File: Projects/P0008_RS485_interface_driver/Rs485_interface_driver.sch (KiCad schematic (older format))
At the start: 6 parts, among them J1 22-05-7045, J2 22-05-7045, U1 SN65176BDR, U2 78L05

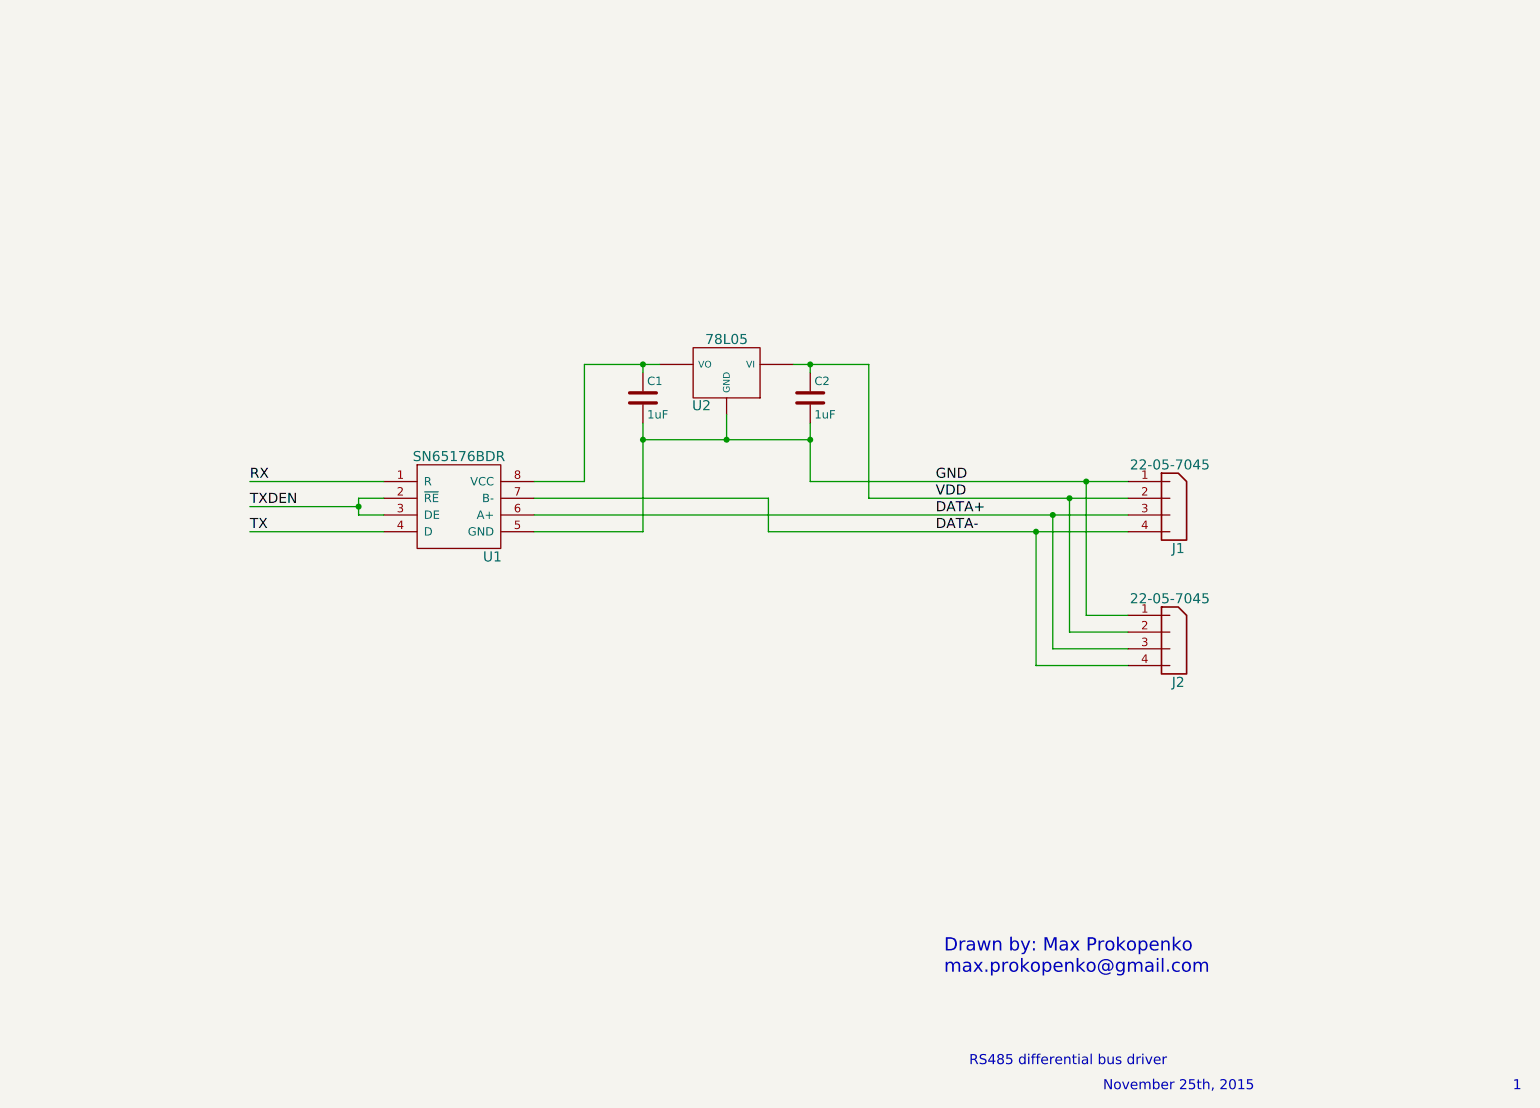
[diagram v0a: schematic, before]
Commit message: finishing routing on bus adapter
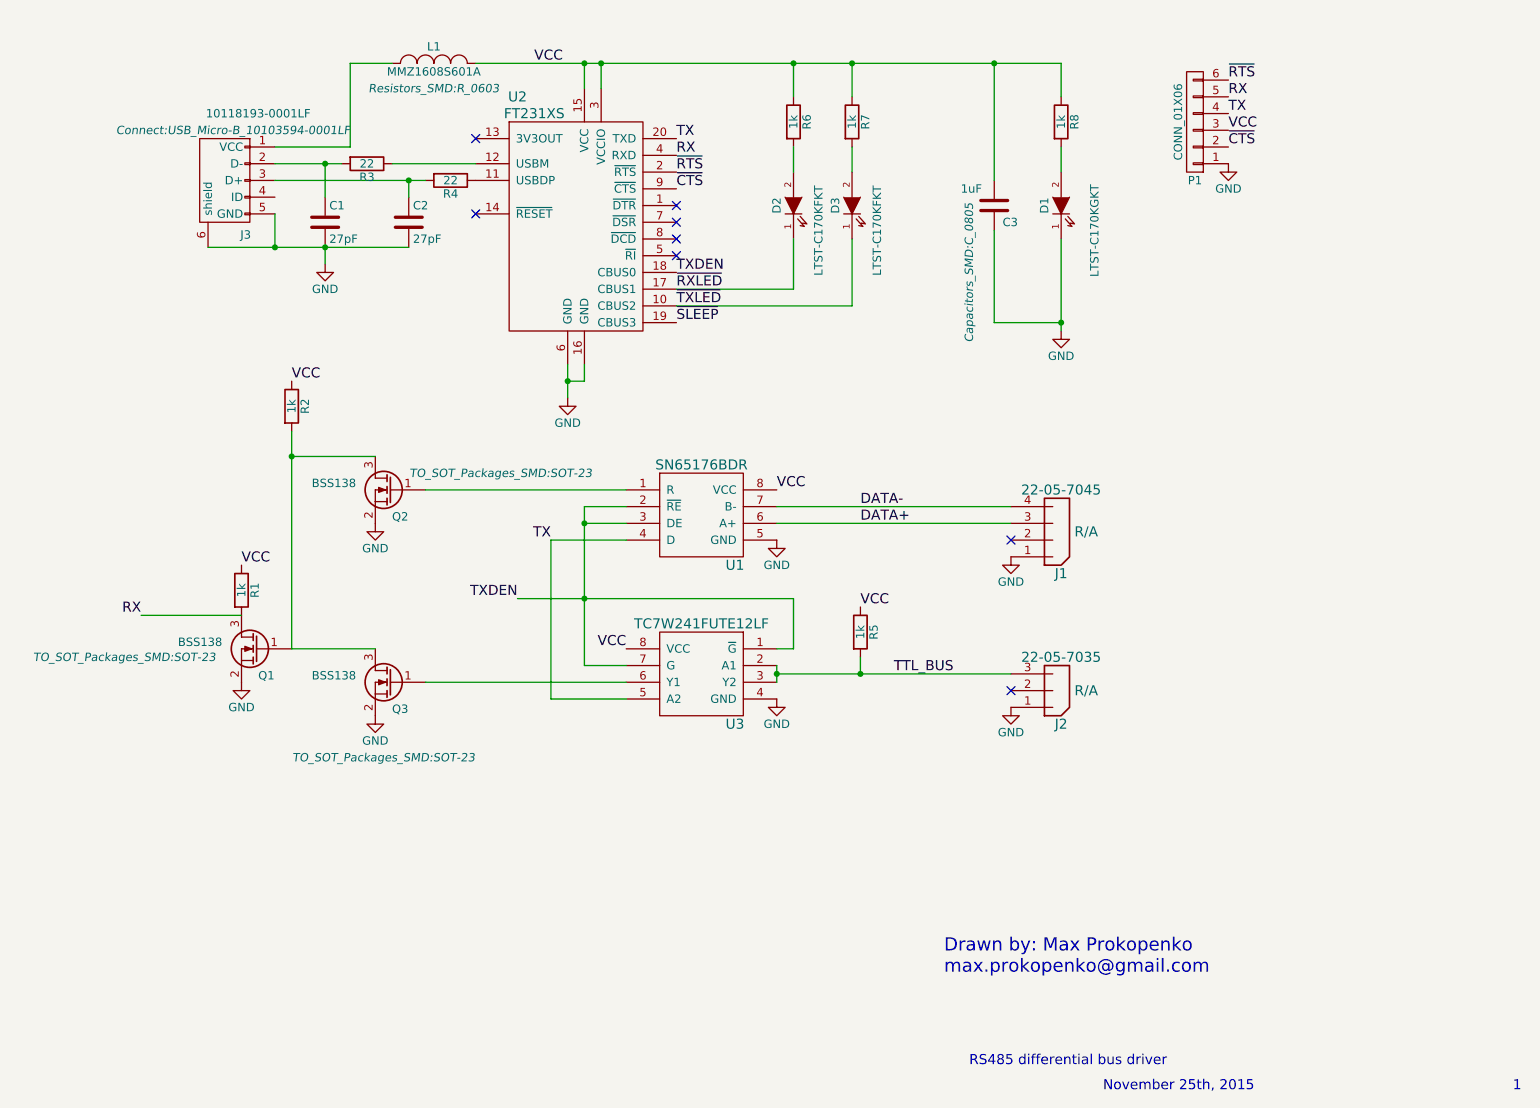
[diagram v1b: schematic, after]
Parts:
- removed J2: 22-05-7045, symbol 22-05-7045
- removed U2: 78L05, symbol 78L05
- added C3: 1uF, Capacitors_SMD:C_0805, symbol C
- added D1: LTST-C170KGKT, LEDs:LED_0805, symbol LTST-C170KGKT
- added D2, D3: LTST-C170KFKT, LEDs:LED_0805, symbol LTST-C170KFKT
- added J2: 22-05-7035, Pin_Headers:Pin_Header_Angled_1x03, symbol 22-05-7035
- added J3: 10118193-0001LF, Connect:USB_Micro-B_10103594-0001LF, symbol 10118193-0001LF
- added L1: MMZ1608S601A, Resistors_SMD:R_0603, symbol MMZ1608S601A
- added P1: CONN_01X06, Pin_Headers:Pin_Header_Straight_1x06, symbol CONN_01X06
- added Q1, Q2, Q3: BSS138, TO_SOT_Packages_SMD:SOT-23, symbol BSS138
- added R1, R2, R5, R6, R7, R8: 1k, Resistors_SMD:R_0805, symbol R
- added R3, R4: 22, Resistors_SMD:R_0805, symbol R
- added U2: FT231XS, SMD_Packages:SSOP-20, symbol FT231XS
- added U3: TC7W241FUTE12LF, Housings_SSOP:MSOP-8_3x3mm_Pitch0.65mm, symbol TC7W241FUTE12LF
- C1, C2: value 1uF -> 27pF; footprint (none) -> Capacitors_SMD:C_0402
- J1: footprint (none) -> Pin_Headers:Pin_Header_Angled_1x04; Orientation (none) -> R/A
- U1: footprint (none) -> Housings_SOIC:SOIC-8_3.9x4.9mm_Pitch1.27mm
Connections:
- net GND: now also C3.2, D1.1 (K), J2.1, J3.5 (GND), J3.6 (shield), P1.1 (P1), Q1.2 (S), Q2.2 (S), Q3.2 (S), U2.16 (GND), U2.6 (GND), U3.4 (GND)
- net RX: now also P1.5 (P5), Q1.3 (D), R1.2, U2.4 (RXD); no longer U1.1 (R)
- net TX: now also P1.4 (P4), U2.20 (TXD), U3.5 (A2)
- net TXDEN: now also U2.18 (CBUS0), U3.1 (~G), U3.7 (G)
- net at C1.1: now also J3.2 (D-), R3.2; no longer U1.8 (VCC)
- net VDD: no longer names the net of J1.2
- net VDD: no longer C2.1
- new net: Q2.1 (G), U1.1 (R)
- new net: Q3.1 (G), U3.6 (Y1)
- new net: Q1.1 (G), Q2.3 (D), Q3.3 (D), R2.2
- new net: J3.1 (VCC), L1.1
- new net: C2.1, J3.3 (D+), R4.2
- new net: R4.1, U2.11 (USBDP)
- new net: R3.1, U2.12 (USBM)
- new net: D2.2 (A), R6.2
- new net: D3.2 (A), R7.2
- new net: D1.2 (A), R8.2
- new net TTL_BUS: J2.3, R5.2, U3.2 (A1), U3.3 (Y2)
- new net VCC: C3.1, L1.2, P1.3 (P3), R1.1, R2.1, R5.1, R6.1, R7.1, R8.1, U1.8 (VCC), U2.15 (VCC), U2.3 (VCCIO), U3.8 (VCC)
- new net ~CTS: P1.2 (P2), U2.9 (~CTS)
- new net ~RTS: P1.6 (P6), U2.2 (~RTS)
- new net ~RXLED: D2.1 (K), U2.17 (CBUS1)
- new net ~SLEEP: U2.19 (CBUS3)
- new net ~TXLED: D3.1 (K), U2.10 (CBUS2)
- no-connect marks 0 -> 8
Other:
- moved on the sheet: U1

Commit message: revised P0008, added gerbers
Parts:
- removed Q2, Q3: BSS138, TO_SOT_Packages_SMD:SOT-23, symbol BSS138
- added Q2, Q3, Q4: BSS84, TO_SOT_Packages_SMD:SOT-23, symbol BSS84
- added R9: 1k, Resistors_SMD:R_0805, symbol R
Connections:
- net GND: now also R2.2
- net RX: no longer P1.5 (P5)
- net VCC: now also Q2.2 (S), Q3.2 (S), Q4.2 (S), R9.1; no longer R2.1
- net at U1.1 (R): now also Q3.1 (G)
- net at U3.6 (Y1): now also Q4.1 (G)
- net at Q1.1 (G): now also R2.1, Q2.3 (D), Q3.3 (D), Q4.3 (D); no longer R2.2
- new net RX_HEADER: P1.5 (P5), Q2.1 (G), R9.2
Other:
- note added: "RS485 and TTL bus to USB interface"
- note removed: "RS485 differential bus driver"
- moved on the sheet: J1, J2, Q1, R1, R2, R5, U1, U3

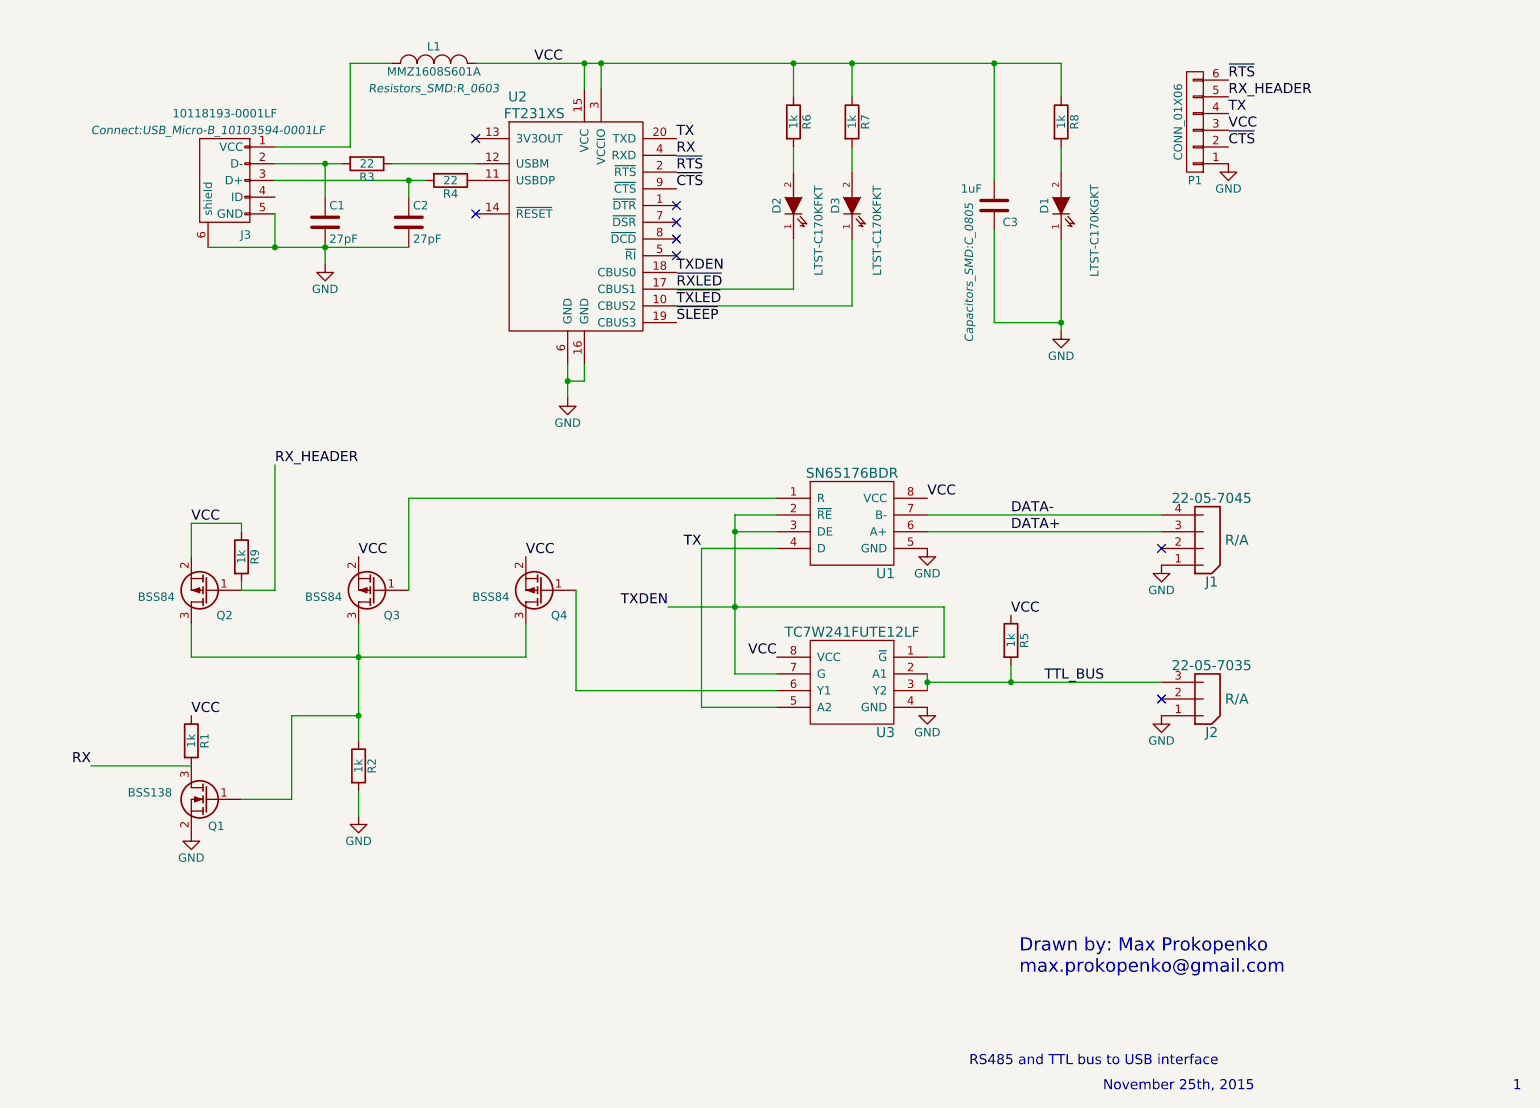
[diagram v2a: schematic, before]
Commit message: Updated pdf for RS485 interface driver
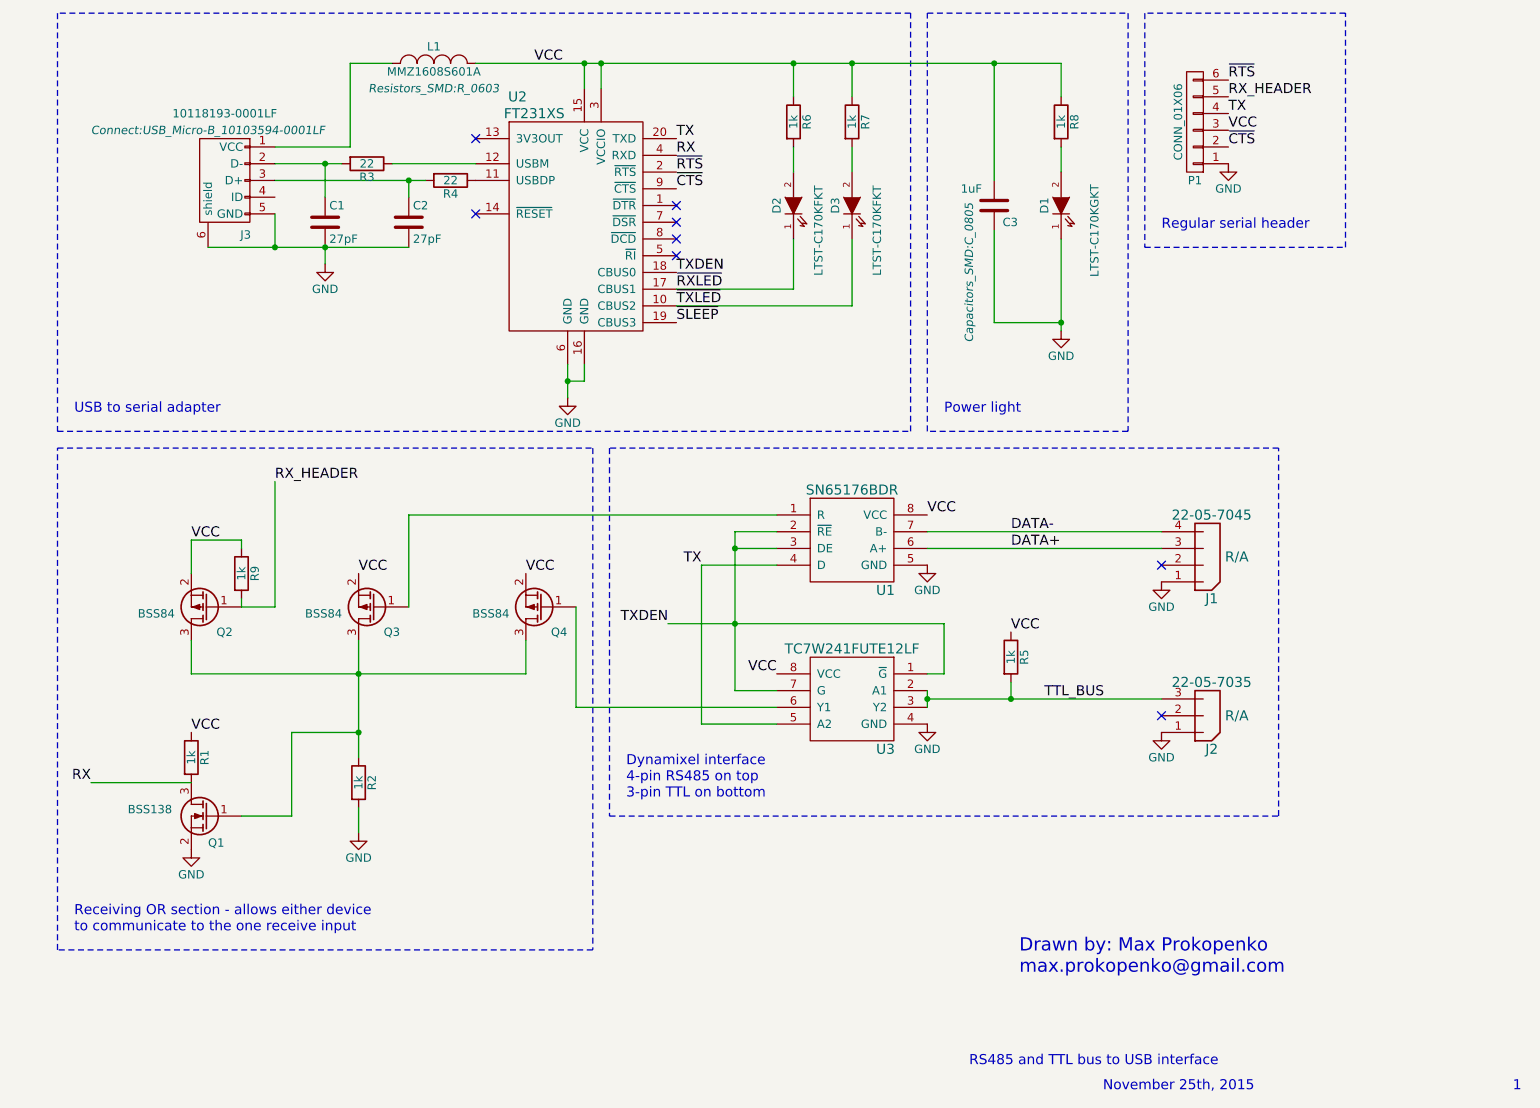
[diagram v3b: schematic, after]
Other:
- note added: "Dynamixel interface\n4-pin RS485 on top\n3-pin TTL on bottom"
- note added: "Power light"
- note added: "Receiving OR section - allows either device\nto communicate to the one receive input"
- note added: "Regular serial header"
- note added: "USB to serial adapter"
- moved on the sheet: J1, J2, Q1, Q2, Q3, Q4, R1, R2, R5, R9, U1, U3
